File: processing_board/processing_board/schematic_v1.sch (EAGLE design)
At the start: 76 parts, among them Q1 BSS138, Q2 BSS138, Q3 BSS138, Q4 BSS138, U1 SN74ALS166D, U2 ATMEGA328P_TQFP, Y1 16MHz

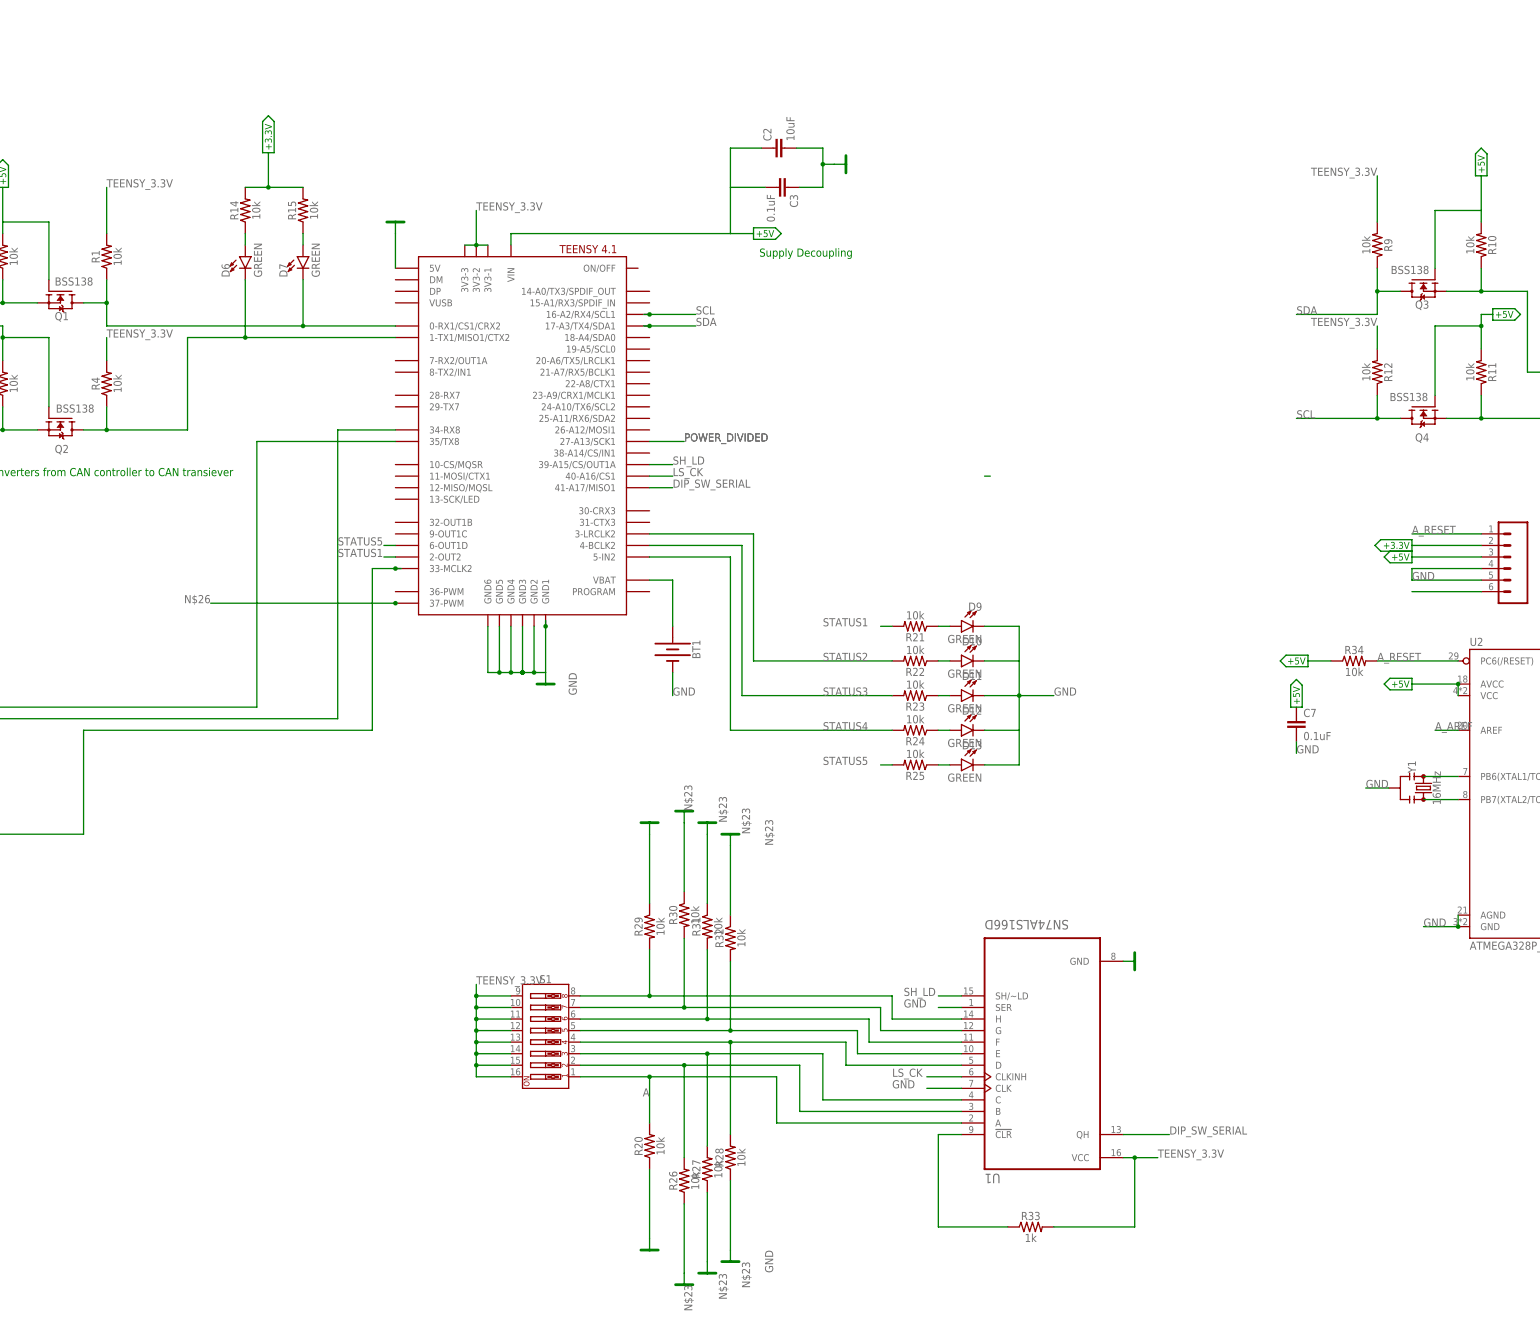
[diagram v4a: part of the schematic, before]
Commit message: updated shif register
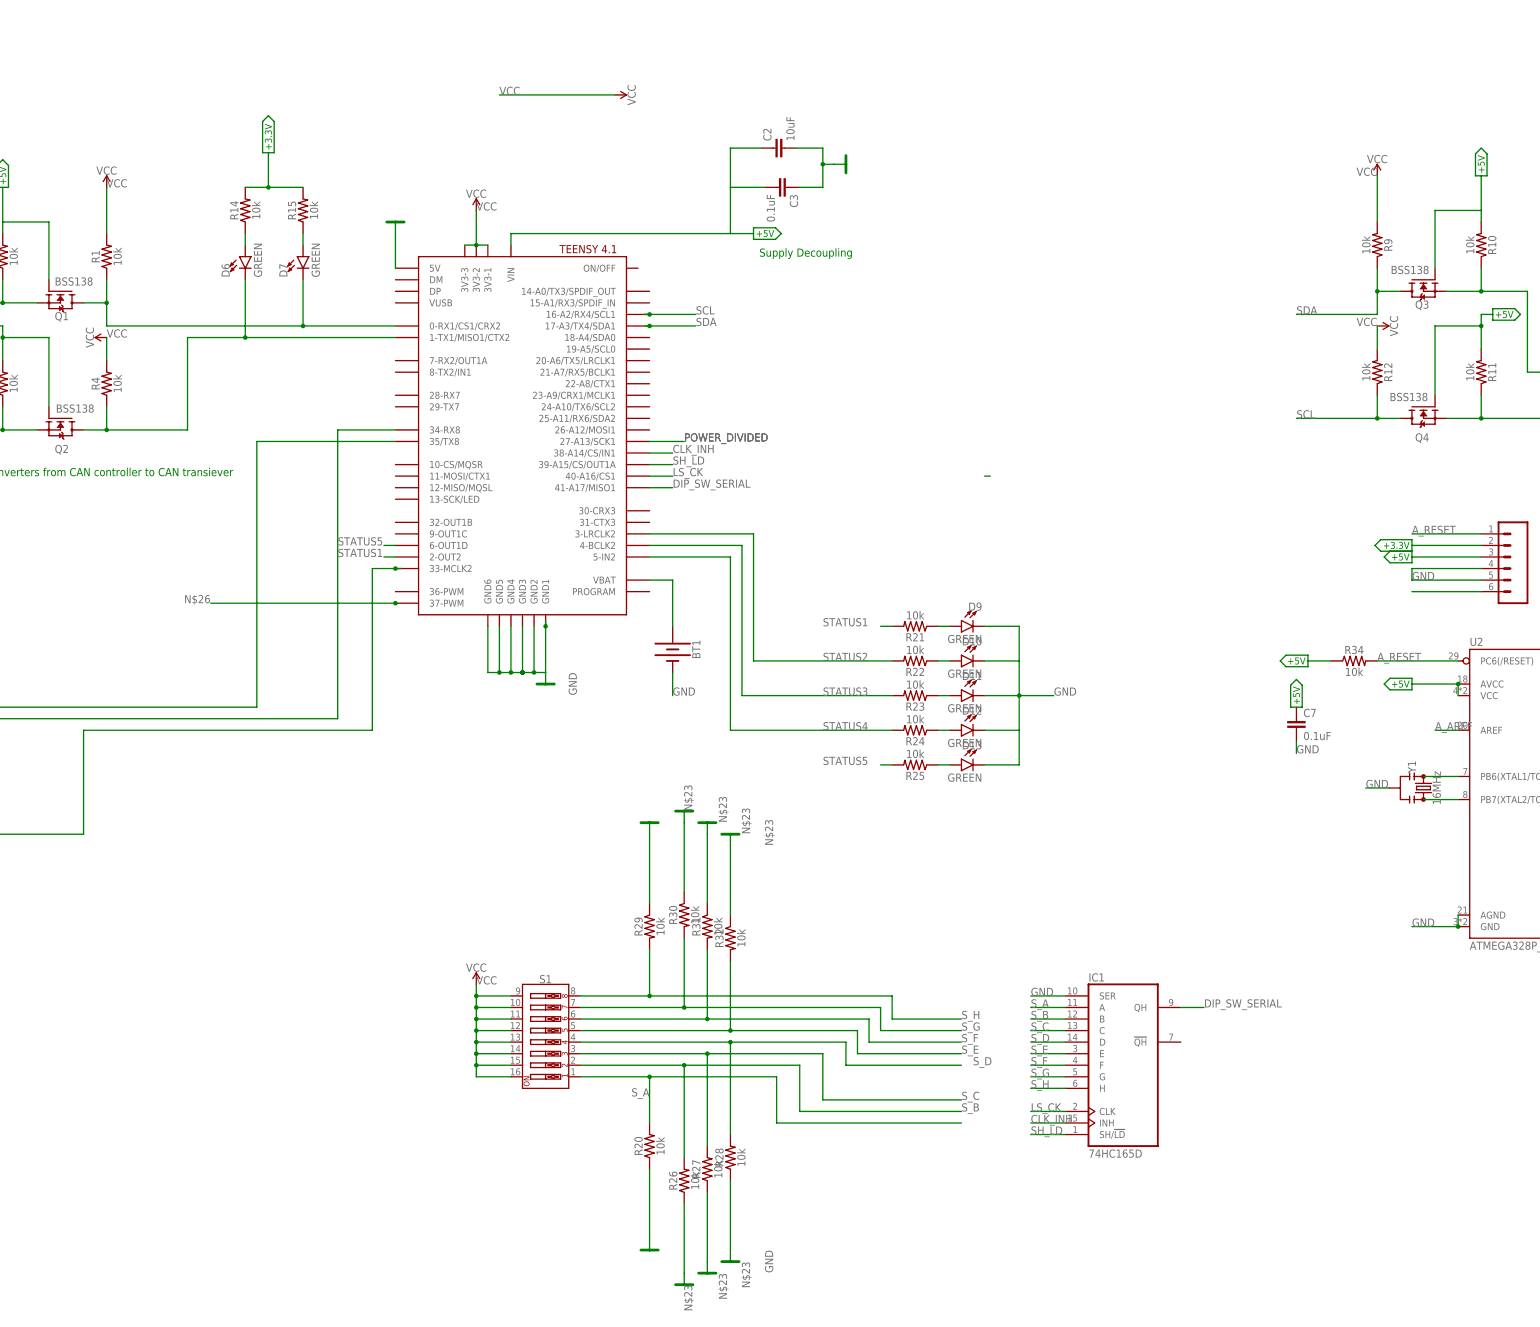
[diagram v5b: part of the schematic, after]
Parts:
- removed R33: 1k, SparkFun-Resistors:1KOHM-0603-1/10W-1%
- removed U1: SN74ALS166D, SN74ALS166D - TI level shifter:SN74ALS166D
- added IC1: 74HC165D, 74xx-eu:74HC165D
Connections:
- removed net A: R20.2, S1.1, U1.A
- removed net C: R27.2, S1.3, U1.C
- removed net D: R28.2, S1.4, U1.D
- removed net E: R32.2, S1.5, U1.E
- removed net H: R29.2, S1.8, U1.H
- removed net N$25: R31.2, S1.6, U1.F
- removed net N$27: R33.1, U1.!CLR
- removed net N$30: R26.2, S1.2, U1.B
- removed net N$9: R30.2, S1.7, U1.G
- removed net TEENSY_3.3V: R1.2, R12.2, R33.2, R4.2, R9.2, S1.10, S1.11, S1.12, S1.13, S1.14, S1.15, S1.16, S1.9, U$4.3V3-1, U$4.3V3-2, U$4.3V3-3, U1.VCC
- new net CLK_INH: IC1A.INH, U$4.38-A14/CS/IN1
- new net S_A: IC1A.A, R20.2, S1.1
- new net S_B: IC1A.B, R26.2, S1.2
- new net S_C: IC1A.C, R27.2, S1.3
- new net S_D: IC1A.D, R28.2, S1.4
- new net S_E: IC1A.E, R32.2, S1.5
- new net S_F: IC1A.F, R31.2, S1.6
- new net S_G: IC1A.G, R30.2, S1.7
- new net S_H: IC1A.H, R29.2, S1.8
- new net VCC: R1.2, R12.2, R4.2, R9.2, S1.10, S1.11, S1.12, S1.13, S1.14, S1.15, S1.16, S1.9, U$4.3V3-1, U$4.3V3-2, U$4.3V3-3
- net DIP_SW_SERIAL: now also IC1A.QH; no longer U1.QH
- net GND: now also IC1A.SER; no longer U1.CLK, U1.GND, U1.SER
- net LS_CK: now also IC1A.CLK; no longer U1.CLKINH
- net SH_LD: now also IC1A.SH/!LD; no longer U1.SH/~LD

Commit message: updated board
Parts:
- removed AD, A_PWR: (no value), SparkFun-Connectors:CONN_06SILK_FEMALE_PTH
- removed BT1: (no value), SparkFun-Batteries:BATTERY-20MM_SMD
- removed C7: 0.1uF, SparkFun-Capacitors:0.1UF-0603-25V-(+80/-20%)
- removed IOH, IOL: (no value), SparkFun-Connectors:CONN_08NO_SILK_FEMALE_PTH
- removed JP1: (no value), pinhead:PINHD-1X14
- removed JP3: (no value), pinhead:PINHD-1X16
- removed JP4: (no value), pinhead:PINHD-2X3
- removed R34: 10k, SparkFun-Resistors:1KOHM-0603-1/10W-1%
- removed U2: ATMEGA328P_TQFP, SparkFun-IC-Microcontroller:ATMEGA328P_TQFP
- removed Y1: 16MHz, SparkFun-Clocks:RESONATOR-16MHZSMD_3.2X1.3
- added U$1: XBEE_SX_PRO, xbee_sx_pro:XBEE_SX_PRO
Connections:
- removed net A_A0: AD.1, U2.PC0(ADC0)
- removed net A_AREF: IOH.8, U2.AREF
- removed net A_MISO: IOH.5, JP4.1, U2.PB4(MISO)
- removed net A_MOSI: IOH.4, JP4.4, U2.PB3(MOSI/OC2)
- removed net A_RESET: A_PWR.1, JP4.5, R34.2, U2.PC6(/RESET)
- removed net A_SCK: IOH.6, JP4.3, U2.PB5(SCK)
- removed net A_SS: IOH.3, U2.PB2(SS/OC1B)
- removed net N$1: D5.C, JP1.5, U$4.35/TX8
- removed net N$2: D2.C, JP1.4, U$4.34-RX8
- removed net N$26: JP1.11, U$4.33-MCLK2
- removed net N$29: AD.2, U2.PC1(ADC1)
- removed net N$3: D8.A, JP1.13
- removed net N$31: AD.3, U2.PC2(ADC2)
- removed net N$32: AD.4, U2.PC3(ADC3)
- removed net N$33: BT1.+, U$4.VBAT
- removed net N$35: IOH.2, U2.PB1(OC1A)
- removed net N$36: IOH.1, U2.PB0(ICP)
- removed net N$37: IOL.8, U2.PD7(AIN1)
- removed net N$38: IOL.7, U2.PD6(AIN0)
- removed net N$39: IOL.6, U2.PD5(T1)
- removed net N$40: IOL.5, U2.PD4(XCK/T0)
- removed net N$41: IOL.4, U2.PD3(INT1)
- removed net N$42: IOL.3, U2.PD2(INT0)
- removed net N$43: IOL.2, U2.PD1(TXD)
- removed net N$45: U2.PB6(XTAL1/TOSC1), Y1.1
- removed net N$46: U2.PB7(XTAL2/TOSC2), Y1.3
- removed net N$50: A_PWR.6
- removed net RESET_: JP1.7
- removed net RXD: IOL.1, U2.PD0(RXD)
- new net DIN: D5.C, U$1.DIO14/DIN/CONFIG, U$4.35/TX8
- new net DOUT: D2.C, U$1.DIO13/DOUT, U$4.34-RX8
- new net EXTRA: U$1.DIO8, U$4.33-MCLK2
- new net N$12: D8.A, U$1.DIO19
- new net RESET: U$1.RESET, U$4.32-OUT1B
- net +3.3V: now also U$1.VCC, U$4.3V3-1, U$4.3V3-2, U$4.3V3-3; no longer A_PWR.2, JP1.3
- net +5V: now also U$4.5V; no longer A_PWR.3, C7.1, JP4.2, R34.1, U2.AVCC, U2.VCC
- net GND: now also U$1.GND@0, U$1.GND@1, U$1.GND@2, U$1.GND@3, U$1.GND@4, U$1.GND@5; no longer A_PWR.4, A_PWR.5, BT1.-, C7.2, IOH.7, JP1.1, JP1.12, JP1.14, JP1.2, JP3.16, JP3.3, JP4.6, U$4.5V, U2.AGND, U2.GND, Y1.2
- net SCL_BUS: no longer AD.6, U2.PC5(ADC5/SCL)
- net SDA_BUS: no longer AD.5, U2.PC4(ADC4/SDA)
- net VCC: no longer U$4.3V3-1, U$4.3V3-2, U$4.3V3-3
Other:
- note removed: "Pin 1"
- note removed: "Pin 37"
- note removed: "pin 15"
- moved on the sheet: D8, R17

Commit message: 3/5 updates
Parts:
- added J1: (no value), SparkFun-Connectors:CONN_02
- added J6: (no value), SparkFun-Connectors:CONN_08"
- added J7, J8: (no value), SparkFun-Connectors:CONN_06NO_SILK_FEMALE_PTH
- added U$5: ARDUINOUNO, adafruit:ARDUINOUNO
- added U1: TJA1050, TJA1050:TJA1050
- J3: device SparkFun-Connectors:CONN_04PTH -> SparkFun-Connectors:CONN_08"
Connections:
- new net N$1: J1.2, U1.CANL
- new net N$2: J1.1, U1.CANH
- net +3.3V: now also J8.5
- net +5V: now also J8.1, J8.4, U1.VCC, U1.VREF; no longer J3.1
- net CAN_RX: now also U1.RXD; no longer J3.3
- net CAN_TX: now also U1.TXD; no longer J3.2
- net GND: now also J8.2, J8.3, U1.GND, U1.S; no longer J3.4
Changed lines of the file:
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@@
 <part name="PWR7" library="supply" deviceset="+5V" device=""/>
 <part name="PWR8" library="supply" deviceset="+5V" device=""/>
-<part name="J3" library="SparkFun-Connectors" deviceset="CONN_04" device="PTH"/>
 <part name="GND8" library="supply" deviceset="GND" device=""/>
 <part name="PWR9" library="supply" deviceset="+5V" device=""/>
@@
 <part name="PWR17" library="supply" deviceset="+3.3V" device=""/>
 <part name="PWR18" library="supply" deviceset="+3.3V" device=""/>
+<part name="U$5" library="adafruit" deviceset="ARDUINO" device="UNO"/>
+<part name="U1" library="TJA1050" deviceset="TJA1050" device=""/>
+<part name="PWR21" library="supply" deviceset="+5V" device=""/>
+<part name="GND5" library="supply" deviceset="GND" device=""/>
+<part name="J1" library="SparkFun-Connectors" deviceset="CONN_02" device=""/>
+<part name="J3" library="SparkFun-Connectors" deviceset="CONN_08" device="&quot;"/>
+<part name="J6" library="SparkFun-Connectors" deviceset="CONN_08" device="&quot;"/>
+<part name="J7" library="SparkFun-Connectors" deviceset="CONN_06" device="NO_SILK_FEMALE_PTH"/>
+<part name="J8" library="SparkFun-Connectors" deviceset="CONN_06" device="NO_SILK_FEMALE_PTH"/>
+<part name="PWR22" library="supply" deviceset="+5V" device=""/>
+<part name="PWR23" library="supply" deviceset="+3.3V" device=""/>
 </parts>
 <sheets>
@@
 <instance part="PWR7" gate="G$1" x="-88.9" y="63.5" smashed="yes" rot="R90" grouprefs="CAN_BUS"/>
 <instance part="PWR8" gate="G$1" x="78.74" y="83.82" smashed="yes" rot="R270"/>
-<instance part="J3" gate="J1" x="-121.92" y="55.88" smashed="yes" grouprefs="CAN_BUS">
-<attribute name="VALUE" x="-127" y="48.514" size="1.778" layer="96" font="vector"/>
-<attribute name="NAME" x="-127" y="64.008" size="1.778" layer="95" font="vector"/>
-</instance>
 <instance part="GND8" gate="VR1" x="-109.22" y="68.58" smashed="yes" rot="R180" grouprefs="CAN_BUS"/>
-<instance part="PWR9" gate="G$1" x="-109.22" y="45.72" smashed="yes" rot="R180" grouprefs="CAN_BUS"/>
+<instance part="PWR9" gate="G$1" x="-121.92" y="63.5" smashed="yes" rot="R270" grouprefs="CAN_BUS"/>
 <instance part="J4" gate="G$1" x="297.18" y="55.88" smashed="yes" rot="R180" grouprefs="I2C">
 <attribute name="VALUE" x="302.26" y="61.214" size="1.778" layer="96" font="vector" rot="R180" align="top-left"/>
@@
 <instance part="PWR17" gate="G$1" x="17.78" y="88.9" smashed="yes"/>
 <instance part="PWR18" gate="G$1" x="-203.2" y="-25.4" smashed="yes"/>
+<instance part="U$5" gate="G$1" x="220.98" y="-27.94" smashed="yes" rot="R90"/>
+<instance part="U1" gate="G$1" x="-142.24" y="58.42" smashed="yes" rot="R180">
+<attribute name="NAME" x="-132.08" y="48.26" size="1.27" layer="95" rot="R180"/>
+<attribute name="VALUE" x="-132.08" y="68.58" size="1.27" layer="96" rot="R180"/>
+</instance>
+<instance part="PWR21" gate="G$1" x="-142.24" y="40.64" smashed="yes" rot="R180"/>
+<instance part="GND5" gate="VR1" x="-142.24" y="78.74" smashed="yes" rot="R180"/>
+<instance part="J1" gate="G$1" x="-172.72" y="55.88" smashed="yes">
+<attribute name="VALUE" x="-175.26" y="51.054" size="1.778" layer="96" font="vector"/>
+<attribute name="NAME" x="-175.26" y="61.468" size="1.778" layer="95" font="vector"/>
+</instance>
+<instance part="J3" gate="G$1" x="177.8" y="-7.62" smashed="yes">
+<attribute name="VALUE" x="172.72" y="-20.066" size="1.778" layer="96" font="vector"/>
+<attribute name="NAME" x="172.72" y="5.588" size="1.778" layer="95" font="vector"/>
+</instance>
+<instance part="J6" gate="G$1" x="177.8" y="-30.48" smashed="yes">
+<attribute name="VALUE" x="172.72" y="-42.926" size="1.778" layer="96" font="vector"/>
+<attribute name="NAME" x="172.72" y="-17.272" size="1.778" layer="95" font="vector"/>
+</instance>
+<instance part="J7" gate="G$1" x="281.94" y="0" smashed="yes" rot="R180">
+<attribute name="VALUE" x="287.02" y="9.906" size="1.778" layer="96" font="vector" rot="R180"/>
+<attribute name="NAME" x="287.02" y="-10.668" size="1.778" layer="95" font="vector" rot="R180"/>
+</instance>
+<instance part="J8" gate="G$1" x="294.64" y="-17.78" smashed="yes" rot="R180">
+<attribute name="VALUE" x="299.72" y="-7.874" size="1.778" layer="96" font="vector" rot="R180"/>
+<attribute name="NAME" x="299.72" y="-28.448" size="1.778" layer="95" font="vector" rot="R180"/>
+</instance>
+<instance part="PWR22" gate="G$1" x="279.4" y="-20.32" smashed="yes" rot="MR270"/>
+<instance part="PWR23" gate="G$1" x="279.4" y="-22.86" smashed="yes" rot="MR270"/>
 </instances>
 <busses>
@@
 </segment>
 <segment>
-<pinref part="J3" gate="J1" pin="4"/>
-<wire x1="-116.84" y1="60.96" x2="-109.22" y2="60.96" width="0.1524" layer="91" grouprefs="CAN_BUS"/>
-<wire x1="-109.22" y1="60.96" x2="-109.22" y2="66.04" width="0.1524" layer="91" grouprefs="CAN_BUS"/>
 <pinref part="GND8" gate="VR1" pin="GND"/>
+<wire x1="-109.22" y1="60.96" x2="-109.22" y2="66.04" width="0.1524" layer="91"/>
+<pinref part="U1" gate="G$1" pin="S"/>
+<wire x1="-109.22" y1="60.96" x2="-129.54" y2="60.96" width="0.1524" layer="91"/>
 </segment>
 <segment>
@@
 <wire x1="-190.5" y1="-50.8" x2="-187.96" y2="-50.8" width="0.1524" layer="91"/>
 </segment>
+<segment>
+<pinref part="U1" gate="G$1" pin="GND"/>
+<wire x1="-142.24" y1="68.58" x2="-142.24" y2="76.2" width="0.1524" layer="91"/>
+<pinref part="GND5" gate="VR1" pin="GND"/>
+</segment>
+<segment>
+<wire x1="289.56" y1="-15.24" x2="289.56" y2="-17.78" width="0.1524" layer="91"/>
+<wire x1="289.56" y1="-17.78" x2="279.4" y2="-17.78" width="0.1524" layer="91"/>
+<junction x="289.56" y="-17.78"/>
+<label x="279.4" y="-17.78" size="1.778" layer="95" rot="MR0"/>
+<pinref part="J8" gate="G$1" pin="2"/>
+<pinref part="J8" gate="G$1" pin="3"/>
+</segment>
 </net>
 <net name="+15V" class="0">
@@
 </segment>
 <segment>
-<pinref part="J3" gate="J1" pin="1"/>
-<wire x1="-116.84" y1="53.34" x2="-109.22" y2="53.34" width="0.1524" layer="91" grouprefs="CAN_BUS"/>
-<wire x1="-109.22" y1="53.34" x2="-109.22" y2="45.72" width="0.1524" layer="91" grouprefs="CAN_BUS"/>
+<wire x1="-129.54" y1="63.5" x2="-121.92" y2="63.5" width="0.1524" layer="91" grouprefs="CAN_BUS"/>
 <pinref part="PWR9" gate="G$1" pin="+5V"/>
+<pinref part="U1" gate="G$1" pin="VREF"/>
 </segment>
 <segment>
@@
 <wire x1="0" y1="78.74" x2="0" y2="76.2" width="0.1524" layer="91"/>
 </segment>
+<segment>
+<pinref part="U1" gate="G$1" pin="VCC"/>
+<wire x1="-142.24" y1="48.26" x2="-142.24" y2="40.64" width="0.1524" layer="91"/>
+<pinref part="PWR21" gate="G$1" pin="+5V"/>
+</segment>
+<segment>
+<wire x1="289.56" y1="-20.32" x2="284.48" y2="-20.32" width="0.1524" layer="91"/>
+<pinref part="PWR22" gate="G$1" pin="+5V"/>
+<wire x1="284.48" y1="-20.32" x2="279.4" y2="-20.32" width="0.1524" layer="91"/>
+<wire x1="289.56" y1="-12.7" x2="284.48" y2="-12.7" width="0.1524" layer="91"/>
+<wire x1="284.48" y1="-12.7" x2="276.86" y2="-12.7" width="0.1524" layer="91"/>
+<wire x1="284.48" y1="-12.7" x2="284.48" y2="-20.32" width="0.1524" layer="91"/>
+<junction x="284.48" y="-12.7"/>
+<junction x="284.48" y="-20.32"/>
+<pinref part="J8" gate="G$1" pin="1"/>
+<pinref part="J8" gate="G$1" pin="4"/>
+</segment>
 </net>
 <net name="+3.3V" class="0">
@@
 <pinref part="PWR18" gate="G$1" pin="+3.3V"/>
 </segment>
+<segment>
+<wire x1="289.56" y1="-22.86" x2="279.4" y2="-22.86" width="0.1524" layer="91"/>
+<pinref part="PWR23" gate="G$1" pin="+3.3V"/>
+<pinref part="J8" gate="G$1" pin="5"/>
+</segment>
 </net>
 <net name="CAN_RX" class="0">
@@
 <wire x1="-86.36" y1="68.58" x2="-96.52" y2="68.58" width="0.1524" layer="91" grouprefs="CAN_BUS"/>
 <junction x="-86.36" y="68.58" grouprefs="CAN_BUS"/>
-<pinref part="J3" gate="J1" pin="3"/>
-<wire x1="-116.84" y1="58.42" x2="-96.52" y2="58.42" width="0.1524" layer="91" grouprefs="CAN_BUS"/>
+<wire x1="-129.54" y1="58.42" x2="-96.52" y2="58.42" width="0.1524" layer="91" grouprefs="CAN_BUS"/>
 <wire x1="-96.52" y1="58.42" x2="-96.52" y2="68.58" width="0.1524" layer="91" grouprefs="CAN_BUS"/>
 <label x="-99.06" y="60.96" size="1.778" layer="95" rot="R180" grouprefs="CAN_BUS"/>
+<pinref part="U1" gate="G$1" pin="RXD"/>
 </segment>
 </net>
@@
 <wire x1="-86.36" y1="40.64" x2="-96.52" y2="40.64" width="0.1524" layer="91" grouprefs="CAN_BUS"/>
 <junction x="-86.36" y="40.64" grouprefs="CAN_BUS"/>
-<wire x1="-96.52" y1="40.64" x2="-96.52" y2="55.88" width="0.1524" layer="91" grouprefs="CAN_BUS"/>
-<pinref part="J3" gate="J1" pin="2"/>
-<wire x1="-96.52" y1="55.88" x2="-116.84" y2="55.88" width="0.1524" layer="91" grouprefs="CAN_BUS"/>
+<wire x1="-96.52" y1="40.64" x2="-96.52" y2="53.34" width="0.1524" layer="91" grouprefs="CAN_BUS"/>
+<wire x1="-96.52" y1="53.34" x2="-129.54" y2="53.34" width="0.1524" layer="91" grouprefs="CAN_BUS"/>
 <label x="-99.06" y="55.88" size="1.778" layer="95" rot="R180" grouprefs="CAN_BUS"/>
+<pinref part="U1" gate="G$1" pin="TXD"/>
 </segment>
 </net>
@@
 </segment>
 </net>
+<net name="N$1" class="0">
+<segment>
+<pinref part="J1" gate="G$1" pin="2"/>
+<pinref part="U1" gate="G$1" pin="CANL"/>
+<wire x1="-165.1" y1="58.42" x2="-154.94" y2="58.42" width="0.1524" layer="91"/>
+<wire x1="-154.94" y1="58.42" x2="-154.94" y2="63.5" width="0.1524" layer="91"/>
+</segment>
+</net>
+<net name="N$2" class="0">
+<segment>
+<pinref part="U1" gate="G$1" pin="CANH"/>
+<pinref part="J1" gate="G$1" pin="1"/>
+<wire x1="-154.94" y1="53.34" x2="-154.94" y2="55.88" width="0.1524" layer="91"/>
+<wire x1="-154.94" y1="55.88" x2="-165.1" y2="55.88" width="0.1524" layer="91"/>
+</segment>
+</net>
